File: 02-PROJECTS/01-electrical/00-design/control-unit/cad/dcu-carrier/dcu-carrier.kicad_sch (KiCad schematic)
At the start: 165 parts, among them J1 DP-DCU DT13-06PA, J10 Teensy 4.1 socket - 2 x 24 fe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, J11 A/C pressure transducer lead 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, J12 radar alert lead - PLACEHOLDER, J2 DP-DCU-C DT13-08PA, J3 cabin NTC lead, J4 panel ribbon 2x13 IDC, keyed, J5 blower pigtail, J6 servo header, J7 servo header, J8 servo header, J9 DP-DCU-B DT13-12PA, Q1 PMV37ENEA, Q2 PMV37ENEA, Q3 SQ2351ES class, >= 40 V confi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, Q4 MMBT3904, U1 LMR36015FSCQ-Q1, U10 BTT6200-4ESA, U11 DRV8962-Q1, U12 TCA9539-Q1, U13 TCA9539-Q1, U14 BTT6050-1ERA, U15 ADS1115-Q1, U16 TPS7B4250-Q1, U2 TPS54560B-Q1, U3 TCAN1042HVDRQ1, U4 INA180A1, U5 BTS3011TE, U6 BTS3011TE, U7 BTS3011TE, U8 BTS3011TE, U9 BTT6050-1ERA

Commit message: Electrical: the carriers corrected before the order - six TVS diodes drawn backwards, the wake switch's pins swapped, an unconnected zener, the bulk capacitor's value (D-547)
Y42 done; Y44 (an independent read of the boards, and the gate drive of two P-FETs) holds the board order Y18. DU and CU carrier fab zips rebuilt; the earlier ones must not be ordered. The board check now holds transistors and diodes to their makers' pin-outs.

Co-Authored-By: Claude Opus 5.5 <noreply@anthropic.com>
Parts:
- C1, C29, C8: value 100u 63V -> 68u 63V
- C31, C32, C33: value 470u 10V -> 470u 16V
- D2, D4, D7, D8: symbol dcu-carrier:D_TVS -> dcu-carrier:D_TVS_Uni
- Q1, Q2: value PMV37ENEA -> SQ2362CES / PMV37ENEA
- Q3: value SQ2351ES class, >= 40 V confirm -> SQ2361ES; symbol dcu-carrier:Q_PMOS_GDS -> dcu-carrier:Q_PMOS_GSD
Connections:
- net +12V_CMF: now also D4.1 (K); no longer D4.2 (A2)
- net +12V_LOGIC: now also D2.1 (K), Q3.2 (S); no longer D2.2 (A2), Q3.3 (S)
- net GND: now also D2.2 (A), D7.2 (A), D8.2 (A); no longer D2.1 (A1), D7.1 (A1), D8.1 (A1)
- net PGND: now also D4.2 (A); no longer D4.1 (A1)
- net REL_FUEL: now also D8.1 (K); no longer D8.2 (A2)
- net REL_HATCH: now also D7.1 (K); no longer D7.2 (A2)
- net WAKE_OUT: now also Q3.3 (D); no longer Q3.2 (D)
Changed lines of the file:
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@@
 	(title_block
 		(title "DCU carrier - H-002")
-		(rev "0.04")
+		(rev "0.05")
 		(company "RX-7 FB electrical build")
 		(comment 1 "Drawn from the record: 02-PROJECTS/01-electrical/data/dcu_channels.csv, panel_ribbon.csv and cavities DP-DCU / -B / -C. Where this sheet and a row disagree, the row is right.")
@@
 	(wire (pts (xy 118.11 40.64) (xy 120.65 40.64)) (stroke (width 0) (type default)))
 	(label "V12L_RAW" (at 120.65 40.64 0) (effects (font (size 1.27 1.27)) (justify left bottom)))
-	(symbol (lib_id "dcu-carrier:D_TVS") (at 165.1 40.64 0) (unit 1) (body_style 1)
+	(symbol (lib_id "dcu-carrier:D_TVS_Uni") (at 165.1 40.64 0) (unit 1) (body_style 1)
 		(exclude_from_sim no) (in_bom yes) (on_board yes) (in_pos_files yes) (dnp no)
 		(property "Reference" "D2" (at 168.1 39.44 0) (effects (font (size 1.1 1.1)) (justify left)))
@@
 		(exclude_from_sim no) (in_bom yes) (on_board yes) (in_pos_files yes) (dnp no)
 		(property "Reference" "C1" (at 208.74 62.3 0) (effects (font (size 1.1 1.1)) (justify left)))
-		(property "Value" "100u 63V" (at 208.74 65.1 0) (effects (font (size 1.1 1.1)) (justify left)))
+		(property "Value" "68u 63V" (at 208.74 65.1 0) (effects (font (size 1.1 1.1)) (justify left)))
 		(property "Footprint" "Capacitor_SMD:CP_Elec_8x10" (at 205.74 63.5 0) (effects (font (size 1.1 1.1)) (hide yes)))
 		(property "Datasheet" "" (at 205.74 63.5 0) (effects (font (size 1.1 1.1)) (hide yes)))
@@
 	(wire (pts (xy 120.65 104.14) (xy 123.19 104.14)) (stroke (width 0) (type default)))
 	(label "V12C_RAW" (at 123.19 104.14 0) (effects (font (size 1.27 1.27)) (justify left bottom)))
-	(symbol (lib_id "dcu-carrier:D_TVS") (at 185.42 104.14 0) (unit 1) (body_style 1)
+	(symbol (lib_id "dcu-carrier:D_TVS_Uni") (at 185.42 104.14 0) (unit 1) (body_style 1)
 		(exclude_from_sim no) (in_bom yes) (on_board yes) (in_pos_files yes) (dnp no)
 		(property "Reference" "D4" (at 188.42 102.94 0) (effects (font (size 1.1 1.1)) (justify left)))
@@
 		(exclude_from_sim no) (in_bom yes) (on_board yes) (in_pos_files yes) (dnp no)
 		(property "Reference" "C8" (at 226.52 123.26 0) (effects (font (size 1.1 1.1)) (justify left)))
-		(property "Value" "100u 63V" (at 226.52 126.06 0) (effects (font (size 1.1 1.1)) (justify left)))
+		(property "Value" "68u 63V" (at 226.52 126.06 0) (effects (font (size 1.1 1.1)) (justify left)))
 		(property "Footprint" "Capacitor_SMD:CP_Elec_8x10" (at 223.52 124.46 0) (effects (font (size 1.1 1.1)) (hide yes)))
 		(property "Datasheet" "" (at 223.52 124.46 0) (effects (font (size 1.1 1.1)) (hide yes)))
@@
 		(exclude_from_sim no) (in_bom yes) (on_board yes) (in_pos_files yes) (dnp no)
 		(property "Reference" "C29" (at 165.56 549.98 0) (effects (font (size 1.1 1.1)) (justify left)))
-		(property "Value" "100u 63V" (at 165.56 552.78 0) (effects (font (size 1.1 1.1)) (justify left)))
+		(property "Value" "68u 63V" (at 165.56 552.78 0) (effects (font (size 1.1 1.1)) (justify left)))
 		(property "Footprint" "Capacitor_SMD:CP_Elec_8x10" (at 162.56 551.18 0) (effects (font (size 1.1 1.1)) (hide yes)))
 		(property "Datasheet" "" (at 162.56 551.18 0) (effects (font (size 1.1 1.1)) (hide yes)))
@@
 		(exclude_from_sim no) (in_bom yes) (on_board yes) (in_pos_files yes) (dnp no)
 		(property "Reference" "Q1" (at 43.18 621.03 0) (effects (font (size 1.1 1.1))))
-		(property "Value" "PMV37ENEA" (at 43.18 631.19 0) (effects (font (size 1.1 1.1))))
+		(property "Value" "SQ2362CES / PMV37ENEA" (at 43.18 631.19 0) (effects (font (size 1.1 1.1))))
 		(property "Footprint" "Package_TO_SOT_SMD:SOT-23" (at 43.18 627.38 0) (effects (font (size 1.1 1.1)) (hide yes)))
 		(property "Datasheet" "" (at 43.18 627.38 0) (effects (font (size 1.1 1.1)) (hide yes)))
@@
 		(instances (project "dcu-carrier" (path "/9652d84f-b171-4144-b035-f61cf665afb4" (reference "#PWR069") (unit 1))))
 	)
-	(symbol (lib_id "dcu-carrier:D_TVS") (at 127 619.76 0) (unit 1) (body_style 1)
+	(symbol (lib_id "dcu-carrier:D_TVS_Uni") (at 127 619.76 0) (unit 1) (body_style 1)
 		(exclude_from_sim no) (in_bom yes) (on_board yes) (in_pos_files yes) (dnp no)
 		(property "Reference" "D7" (at 130 618.56 0) (effects (font (size 1.1 1.1)) (justify left)))
@@
 		(exclude_from_sim no) (in_bom yes) (on_board yes) (in_pos_files yes) (dnp no)
 		(property "Reference" "Q2" (at 200.66 621.03 0) (effects (font (size 1.1 1.1))))
-		(property "Value" "PMV37ENEA" (at 200.66 631.19 0) (effects (font (size 1.1 1.1))))
+		(property "Value" "SQ2362CES / PMV37ENEA" (at 200.66 631.19 0) (effects (font (size 1.1 1.1))))
 		(property "Footprint" "Package_TO_SOT_SMD:SOT-23" (at 200.66 627.38 0) (effects (font (size 1.1 1.1)) (hide yes)))
 		(property "Datasheet" "" (at 200.66 627.38 0) (effects (font (size 1.1 1.1)) (hide yes)))
@@
 		(instances (project "dcu-carrier" (path "/9652d84f-b171-4144-b035-f61cf665afb4" (reference "#PWR070") (unit 1))))
 	)
-	(symbol (lib_id "dcu-carrier:D_TVS") (at 281.94 619.76 0) (unit 1) (body_style 1)
+	(symbol (lib_id "dcu-carrier:D_TVS_Uni") (at 281.94 619.76 0) (unit 1) (body_style 1)
 		(exclude_from_sim no) (in_bom yes) (on_board yes) (in_pos_files yes) (dnp no)
 		(property "Reference" "D8" (at 284.94 618.56 0) (effects (font (size 1.1 1.1)) (justify left)))
@@
 	(label "REL_FUEL" (at 288.29 619.76 0) (effects (font (size 1.27 1.27)) (justify left bottom)))
 	(text "SN21  wake request: sources 12 V into the PMU wake strip (a diode-OR of 12 V inputs, D-350) - the ICU backlight stage" (exclude_from_sim no) (at 338.67 610.95 0) (effects (font (size 1.5 1.5) (bold yes)) (justify left top)))
-	(symbol (lib_id "dcu-carrier:Q_PMOS_GDS") (at 360.68 640.08 0) (unit 1) (body_style 1)
+	(symbol (lib_id "dcu-carrier:Q_PMOS_GSD") (at 360.68 640.08 0) (unit 1) (body_style 1)
 		(exclude_from_sim no) (in_bom yes) (on_board yes) (in_pos_files yes) (dnp no)
 		(property "Reference" "Q3" (at 363.68 638.88 0) (effects (font (size 1.1 1.1)) (justify left)))
-		(property "Value" "SQ2351ES class, >= 40 V  confirm" (at 363.68 641.68 0) (effects (font (size 1.1 1.1)) (justify left)))
+		(property "Value" "SQ2361ES" (at 363.68 641.68 0) (effects (font (size 1.1 1.1)) (justify left)))
 		(property "Footprint" "Package_TO_SOT_SMD:SOT-23" (at 360.68 640.08 0) (effects (font (size 1.1 1.1)) (hide yes)))
 		(property "Datasheet" "" (at 360.68 640.08 0) (effects (font (size 1.1 1.1)) (hide yes)))
@@
 		(exclude_from_sim no) (in_bom yes) (on_board yes) (in_pos_files yes) (dnp no)
 		(property "Reference" "C31" (at 188.42 710 0) (effects (font (size 1.1 1.1)) (justify left)))
-		(property "Value" "470u 10V" (at 188.42 712.8 0) (effects (font (size 1.1 1.1)) (justify left)))
+		(property "Value" "470u 16V" (at 188.42 712.8 0) (effects (font (size 1.1 1.1)) (justify left)))
 		(property "Footprint" "Capacitor_SMD:CP_Elec_8x10" (at 185.42 711.2 0) (effects (font (size 1.1 1.1)) (hide yes)))
 		(property "Datasheet" "" (at 185.42 711.2 0) (effects (font (size 1.1 1.1)) (hide yes)))
@@
 		(exclude_from_sim no) (in_bom yes) (on_board yes) (in_pos_files yes) (dnp no)
 		(property "Reference" "C32" (at 279.86 710 0) (effects (font (size 1.1 1.1)) (justify left)))
-		(property "Value" "470u 10V" (at 279.86 712.8 0) (effects (font (size 1.1 1.1)) (justify left)))
+		(property "Value" "470u 16V" (at 279.86 712.8 0) (effects (font (size 1.1 1.1)) (justify left)))
 		(property "Footprint" "Capacitor_SMD:CP_Elec_8x10" (at 276.86 711.2 0) (effects (font (size 1.1 1.1)) (hide yes)))
 		(property "Datasheet" "" (at 276.86 711.2 0) (effects (font (size 1.1 1.1)) (hide yes)))
@@
 		(exclude_from_sim no) (in_bom yes) (on_board yes) (in_pos_files yes) (dnp no)
 		(property "Reference" "C33" (at 371.3 710 0) (effects (font (size 1.1 1.1)) (justify left)))
-		(property "Value" "470u 10V" (at 371.3 712.8 0) (effects (font (size 1.1 1.1)) (justify left)))
+		(property "Value" "470u 16V" (at 371.3 712.8 0) (effects (font (size 1.1 1.1)) (justify left)))
 		(property "Footprint" "Capacitor_SMD:CP_Elec_8x10" (at 368.3 711.2 0) (effects (font (size 1.1 1.1)) (hide yes)))
 		(property "Datasheet" "" (at 368.3 711.2 0) (effects (font (size 1.1 1.1)) (hide yes)))

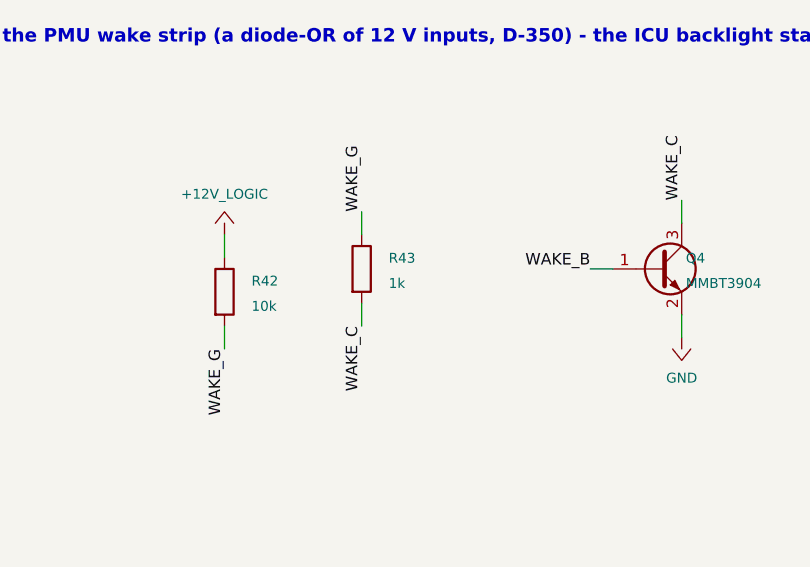
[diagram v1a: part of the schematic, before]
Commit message: Electrical: the two P-FETs' gate drive brought down, the order text names the parts as they are (D-547)
CU Q3: R43 18 k, inside its gate limit at the 53 V clamp. DU Q1: R2 10 k, inside to 40 V on the rail; a gate zener for the clamp case is held for one fix pass with the independent review's findings (Y44). No fab file changed; the cart file follows. Y18's steps rebuilt.

Co-Authored-By: Claude Opus 5.5 <noreply@anthropic.com>
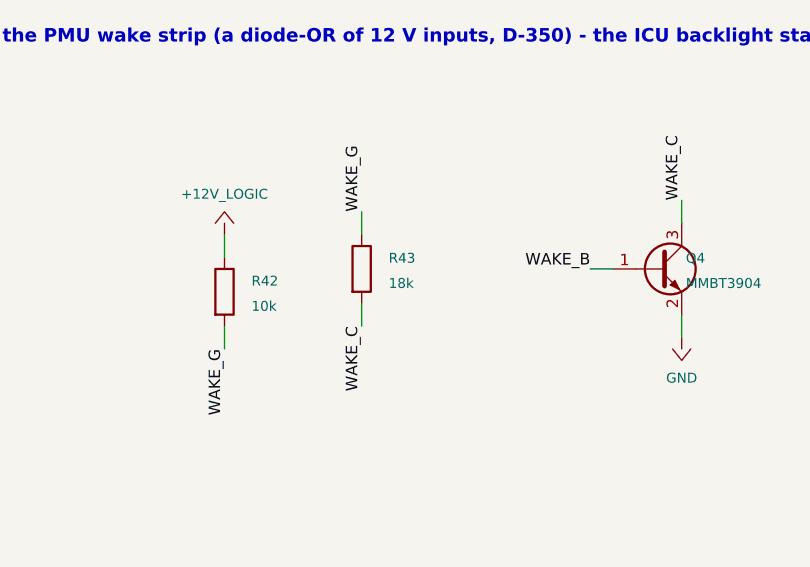
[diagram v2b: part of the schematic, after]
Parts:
- R43: value 1k -> 18k
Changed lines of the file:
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@@
 	(title_block
 		(title "DCU carrier - H-002")
-		(rev "0.05")
+		(rev "0.06")
 		(company "RX-7 FB electrical build")
 		(comment 1 "Drawn from the record: 02-PROJECTS/01-electrical/data/dcu_channels.csv, panel_ribbon.csv and cavities DP-DCU / -B / -C. Where this sheet and a row disagree, the row is right.")
@@
 		(exclude_from_sim no) (in_bom yes) (on_board yes) (in_pos_files yes) (dnp no)
 		(property "Reference" "R43" (at 427.18 636.34 0) (effects (font (size 1.1 1.1)) (justify left)))
-		(property "Value" "1k" (at 427.18 639.14 0) (effects (font (size 1.1 1.1)) (justify left)))
+		(property "Value" "18k" (at 427.18 639.14 0) (effects (font (size 1.1 1.1)) (justify left)))
 		(property "Footprint" "Resistor_SMD:R_0805_2012Metric" (at 424.18 637.54 0) (effects (font (size 1.1 1.1)) (hide yes)))
 		(property "Datasheet" "" (at 424.18 637.54 0) (effects (font (size 1.1 1.1)) (hide yes)))

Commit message: Electrical: the independent read's findings fixed on the boards before the order, and the Display Unit's brake-warning input given its pull-up (D-549)
Y44 done; Y18 (the board order) opens. DU carrier rev 0.06: road-speed input IC08 re-laid, a 15 V gate zener and 4.7 k on the backlight switch, four vias at each backlight layer change, brake warning IC06 pulled up to 3V3 (found while the changes were read back - it could never have read high), tell-tale dividers 22 k, MMBT5551 and SL310A on the rails clamped at 53 V. CU carrier rev 0.07, values only: C27 100 nF, Q1 / Q2 SQ2364EES, Q4 MMBT5551, D1 SL310A. Panel: the encoders' lug slots to Bourns' layout. Two assembly drawings in each fab folder in place of silkscreen references.

ERC 0, DRC 0 / 0 / 0, check.py 0 mismatches on all five boards. The DU carrier's and the panel's fab zips are rebuilt under the same names; the CU carrier's and the upper board's are unchanged. Cart 98 lines. Record: icu_channels IC06 IC08 IC09 IC12 IC13, dcu_channels SN23 SN24, parts P106 P107 P147 P149 P169 P170 P203, Y18 / F3 / F5 briefs and steps. D-548's DT13 question is untouched (V-117).

Co-Authored-By: Claude Opus 5.5 <noreply@anthropic.com>
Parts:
- C27: value 22n 100V confirm -> 100n 100V
- D1: value SS34 -> SL310A
- Q1, Q2: value SQ2362CES / PMV37ENEA -> SQ2364EES
- Q4: value MMBT3904 -> MMBT5551
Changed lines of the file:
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@@
 	(title_block
 		(title "DCU carrier - H-002")
-		(rev "0.06")
+		(rev "0.07")
 		(company "RX-7 FB electrical build")
 		(comment 1 "Drawn from the record: 02-PROJECTS/01-electrical/data/dcu_channels.csv, panel_ribbon.csv and cavities DP-DCU / -B / -C. Where this sheet and a row disagree, the row is right.")
@@
 		(exclude_from_sim no) (in_bom yes) (on_board yes) (in_pos_files yes) (dnp no)
 		(property "Reference" "D1" (at 117.3 39.44 0) (effects (font (size 1.1 1.1)) (justify left)))
-		(property "Value" "SS34" (at 117.3 42.24 0) (effects (font (size 1.1 1.1)) (justify left)))
+		(property "Value" "SL310A" (at 117.3 42.24 0) (effects (font (size 1.1 1.1)) (justify left)))
 		(property "Footprint" "Diode_SMD:D_SMA" (at 114.3 40.64 0) (effects (font (size 1.1 1.1)) (hide yes)))
 		(property "Datasheet" "" (at 114.3 40.64 0) (effects (font (size 1.1 1.1)) (hide yes)))
@@
 		(exclude_from_sim no) (in_bom yes) (on_board yes) (in_pos_files yes) (dnp no)
 		(property "Reference" "C27" (at 119.84 547.44 0) (effects (font (size 1.1 1.1)) (justify left)))
-		(property "Value" "22n 100V  confirm" (at 119.84 550.24 0) (effects (font (size 1.1 1.1)) (justify left)))
+		(property "Value" "100n 100V" (at 119.84 550.24 0) (effects (font (size 1.1 1.1)) (justify left)))
 		(property "Footprint" "Capacitor_SMD:C_0805_2012Metric" (at 116.84 548.64 0) (effects (font (size 1.1 1.1)) (hide yes)))
 		(property "Datasheet" "" (at 116.84 548.64 0) (effects (font (size 1.1 1.1)) (hide yes)))
@@
 		(exclude_from_sim no) (in_bom yes) (on_board yes) (in_pos_files yes) (dnp no)
 		(property "Reference" "Q1" (at 43.18 621.03 0) (effects (font (size 1.1 1.1))))
-		(property "Value" "SQ2362CES / PMV37ENEA" (at 43.18 631.19 0) (effects (font (size 1.1 1.1))))
+		(property "Value" "SQ2364EES" (at 43.18 631.19 0) (effects (font (size 1.1 1.1))))
 		(property "Footprint" "Package_TO_SOT_SMD:SOT-23" (at 43.18 627.38 0) (effects (font (size 1.1 1.1)) (hide yes)))
 		(property "Datasheet" "" (at 43.18 627.38 0) (effects (font (size 1.1 1.1)) (hide yes)))
@@
 		(exclude_from_sim no) (in_bom yes) (on_board yes) (in_pos_files yes) (dnp no)
 		(property "Reference" "Q2" (at 200.66 621.03 0) (effects (font (size 1.1 1.1))))
-		(property "Value" "SQ2362CES / PMV37ENEA" (at 200.66 631.19 0) (effects (font (size 1.1 1.1))))
+		(property "Value" "SQ2364EES" (at 200.66 631.19 0) (effects (font (size 1.1 1.1))))
 		(property "Footprint" "Package_TO_SOT_SMD:SOT-23" (at 200.66 627.38 0) (effects (font (size 1.1 1.1)) (hide yes)))
 		(property "Datasheet" "" (at 200.66 627.38 0) (effects (font (size 1.1 1.1)) (hide yes)))
@@
 		(exclude_from_sim no) (in_bom yes) (on_board yes) (in_pos_files yes) (dnp no)
 		(property "Reference" "Q4" (at 460.2 636.34 0) (effects (font (size 1.1 1.1)) (justify left)))
-		(property "Value" "MMBT3904" (at 460.2 639.14 0) (effects (font (size 1.1 1.1)) (justify left)))
+		(property "Value" "MMBT5551" (at 460.2 639.14 0) (effects (font (size 1.1 1.1)) (justify left)))
 		(property "Footprint" "Package_TO_SOT_SMD:SOT-23" (at 457.2 637.54 0) (effects (font (size 1.1 1.1)) (hide yes)))
 		(property "Datasheet" "" (at 457.2 637.54 0) (effects (font (size 1.1 1.1)) (hide yes)))

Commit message: Electrical: the dash-light stage and the wake on U13 drawn on the DCU sheet; run.sh passes whole (D-577, D-593)
Y49 done on the sheet: U17 BTS3011TE with R73 / R74 / R75, the wake request on U13 P02, the stage's
STATUS on U13 P03; ERC 0, check.py dcu 172 / 0 (it now reads a second expander a cell names). The
board half goes to Y54 with the new header (D-593). With it tests/run.sh passes end to end - every
suite, all four sheets, all six sketches compiled - so F-019 closes. Y51 closed (the CUR's knob).

Co-Authored-By: Claude Opus 5.5 <noreply@anthropic.com>
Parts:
- added R73: 100 dash IN series (SN31), Resistor_SMD:R_0805_2012Metric, symbol dcu-carrier:R
- added R74: 10k dash IN pull-up: full at reset (SN31), Resistor_SMD:R_0805_2012Metric, symbol dcu-carrier:R
- added R75: 10k dash STATUS pull-up (BTS3011TE p.40), Resistor_SMD:R_0805_2012Metric, symbol dcu-carrier:R
- added TP2: DASH_OUT - to DP-DCU 35 at Y54, TestPoint:TestPoint_Pad_2.5x2.5mm, symbol dcu-carrier:TestPoint
- added U17: BTS3011TE, Package_TO_SOT_SMD:TO-252-5_TabPin6, symbol dcu-carrier:BTS3011TE
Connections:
- net +3V3: now also R74.2, R75.2, U17.2 (VDD)
- net PGND: now also U17.5 (GND)
- net WAKE_T: now also U13.6 (P02); no longer J10.13 (11 WAKE_T)
- net DASH_STATUS: now reaches U13.7 (P03)
- net DASH_STATUS: now also R75.1, U17.4 (STATUS)
- new net DASH_IN: R73.2, R74.1, U17.1 (IN)
- new net DASH_OUT: TP2.1, U17.3 (OUT), U17.6 (OUT)
- new net DASH_PWM: J10.13 (11 WAKE_T), R73.1
- no-connect marks 16 -> 14
